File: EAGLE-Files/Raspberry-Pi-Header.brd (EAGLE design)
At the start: 22.8 x 68.2 mm, 3 parts

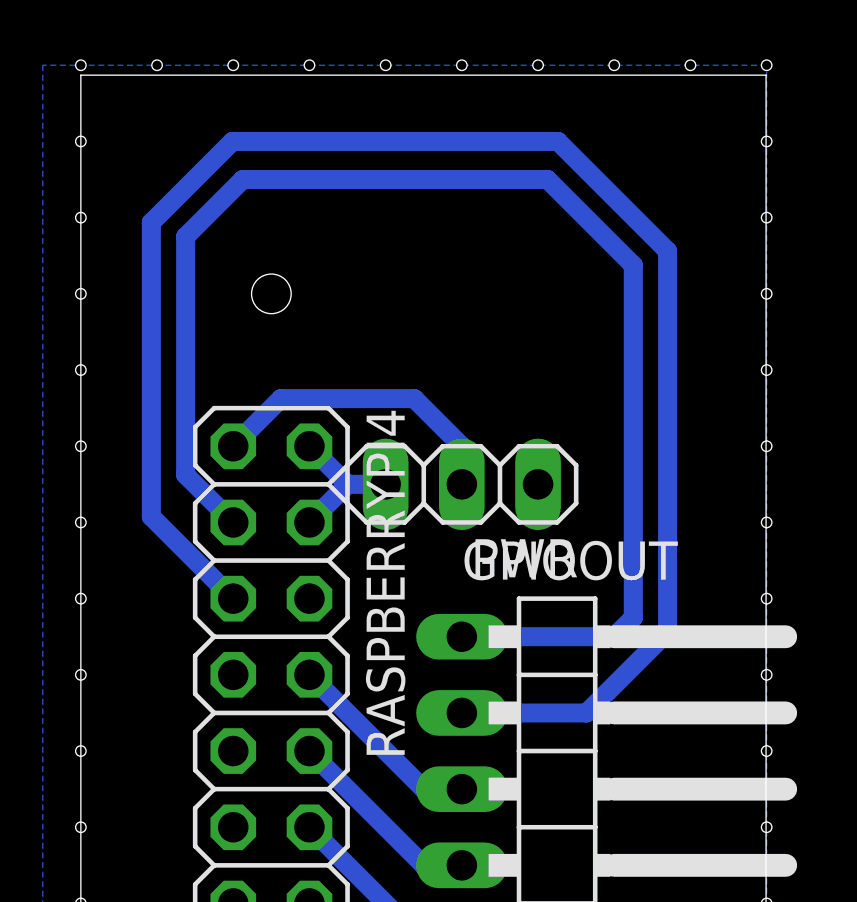
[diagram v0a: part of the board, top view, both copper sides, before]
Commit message: * Updated gitignore * Updated some of the EAGLE boards
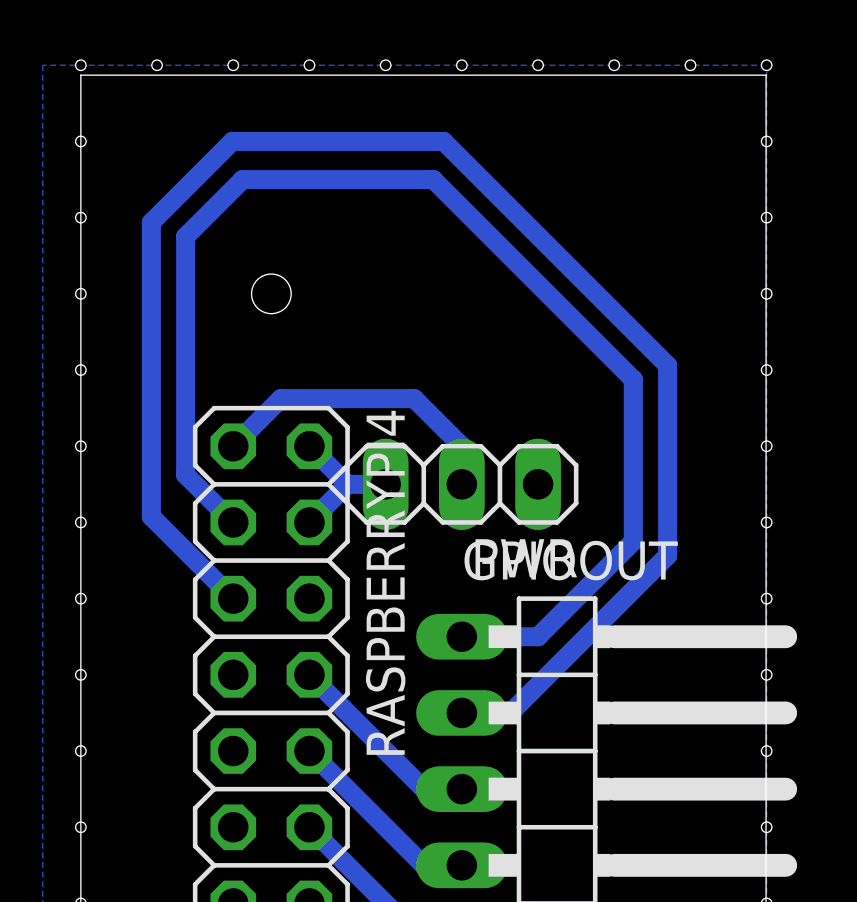
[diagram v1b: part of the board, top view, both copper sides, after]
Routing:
- net SCL: track 54.2 -> 50.5 mm
- net SDA: track 44.8 -> 41.1 mm
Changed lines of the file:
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@@
 <contactref element="RASPBERRYPI4" pad="3"/>
 <contactref element="GPIOOUT" pad="1"/>
-<wire x1="18.415" y1="50.165" x2="17.78" y2="49.53" width="0.635" layer="16"/>
-<wire x1="17.78" y1="49.53" x2="12.7" y2="49.53" width="0.635" layer="16"/>
-<wire x1="18.415" y1="61.9125" x2="18.415" y2="50.165" width="0.635" layer="16"/>
-<wire x1="15.5575" y1="64.77" x2="18.415" y2="61.9125" width="0.635" layer="16"/>
-<wire x1="5.3975" y1="64.77" x2="15.5575" y2="64.77" width="0.635" layer="16"/>
+<wire x1="18.415" y1="52.705" x2="15.24" y2="49.53" width="0.635" layer="16"/>
+<wire x1="15.24" y1="49.53" x2="12.7" y2="49.53" width="0.635" layer="16"/>
+<wire x1="18.415" y1="58.1025" x2="18.415" y2="52.705" width="0.635" layer="16"/>
+<wire x1="11.7475" y1="64.77" x2="18.415" y2="58.1025" width="0.635" layer="16"/>
+<wire x1="5.3975" y1="64.77" x2="11.7475" y2="64.77" width="0.635" layer="16"/>
 <wire x1="3.4925" y1="62.865" x2="5.3975" y2="64.77" width="0.635" layer="16"/>
 <wire x1="3.4925" y1="54.9275" x2="3.4925" y2="62.865" width="0.635" layer="16"/>
@@
 <wire x1="2.3495" y1="63.33845" x2="2.3495" y2="53.5305" width="0.635" layer="16"/>
 <wire x1="2.3495" y1="53.5305" x2="5.08" y2="50.8" width="0.635" layer="16"/>
-<wire x1="5.05105" y1="66.04" x2="15.90395" y2="66.04" width="0.635" layer="16"/>
-<wire x1="15.90395" y1="66.04" x2="19.558" y2="62.38595" width="0.635" layer="16"/>
-<wire x1="19.558" y1="49.69155" x2="16.85645" y2="46.99" width="0.635" layer="16"/>
-<wire x1="16.85645" y1="46.99" x2="12.7" y2="46.99" width="0.635" layer="16"/>
-<wire x1="19.558" y1="62.38595" x2="19.558" y2="49.69155" width="0.635" layer="16"/>
+<wire x1="5.05105" y1="66.04" x2="12.09395" y2="66.04" width="0.635" layer="16"/>
+<wire x1="12.09395" y1="66.04" x2="19.558" y2="58.57595" width="0.635" layer="16"/>
+<wire x1="19.558" y1="52.23155" x2="14.31645" y2="46.99" width="0.635" layer="16"/>
+<wire x1="14.31645" y1="46.99" x2="12.7" y2="46.99" width="0.635" layer="16"/>
+<wire x1="19.558" y1="58.57595" x2="19.558" y2="52.23155" width="0.635" layer="16"/>
 </signal>
 <signal name="GPIO14">
